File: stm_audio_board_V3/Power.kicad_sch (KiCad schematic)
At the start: 100 parts, among them J5 Barrel_Jack_MountingPin, U1 IS42S16100H-7TL, U2 OP275, U3 7909, U4 OP275, U5 MIC2920A-3.3WS-TR, U6 7809, U9 MIC2920A-3.3WS-TR

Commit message: minor commit
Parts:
- removed C2: 47uf, Capacitor_THT:CP_Radial_D6.3mm_P2.50mm, symbol Device:C_Polarized_Small_US
- removed U5: MIC2920A-3.3WS-TR, Package_TO_SOT_SMD:SOT-223-3_TabPin2, symbol Regulator_Linear:LF33_TO252
- removed U9: MIC2920A-3.3WS-TR, Package_TO_SOT_SMD:SOT-89-3, symbol Regulator_Linear:LF33_TO252
- added C30 (x12): 10uF, Capacitor_SMD:C_1206_3216Metric, symbol Device:C_Small
- added C30: 100n, Capacitor_SMD:C_0603_1608Metric, symbol Device:C_Small
- added U20, U5: AP1117-33, Package_TO_SOT_SMD:SOT-223-3_TabPin2, symbol Regulator_Linear:AP1117-33
- C29: value 100uF -> 100uf
- C29: value 47uF -> 100uf
- U3: JLCPCB (none) -> C8623
- U6: JLCPCB (none) -> C5451665
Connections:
- net +3.3V: now also C29.1, C30.1, C30.1, C30.1, U20.2 (VO)
- net +3.3VA: now also C30.1, C30.1, U5.2 (VO)
- net 5V: now also C30.1, C30.1, C30.1, C30.1, C30.1, U20.3 (VI); no longer C29.1
- net GND: now also C30.2, C30.2, C30.2, C30.2, C30.2, C30.2, C30.2, C30.2, C30.2, C30.2, C30.2, C30.2, C30.2, U20.1 (GND), U5.1 (GND)
- net at C29.1, L5.2: now also C30.1, C30.1, C30.1, U5.3 (VI)
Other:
- note removed: "C157412"
- note removed: "L78M09ABDT-TR"
- note removed: "https://jlcpcb.com/partdetail/Stmicroelectronics-L78M09ABDTTR/C157412"
- moved on the sheet: C29, C3, C30, C4, L5, TP6

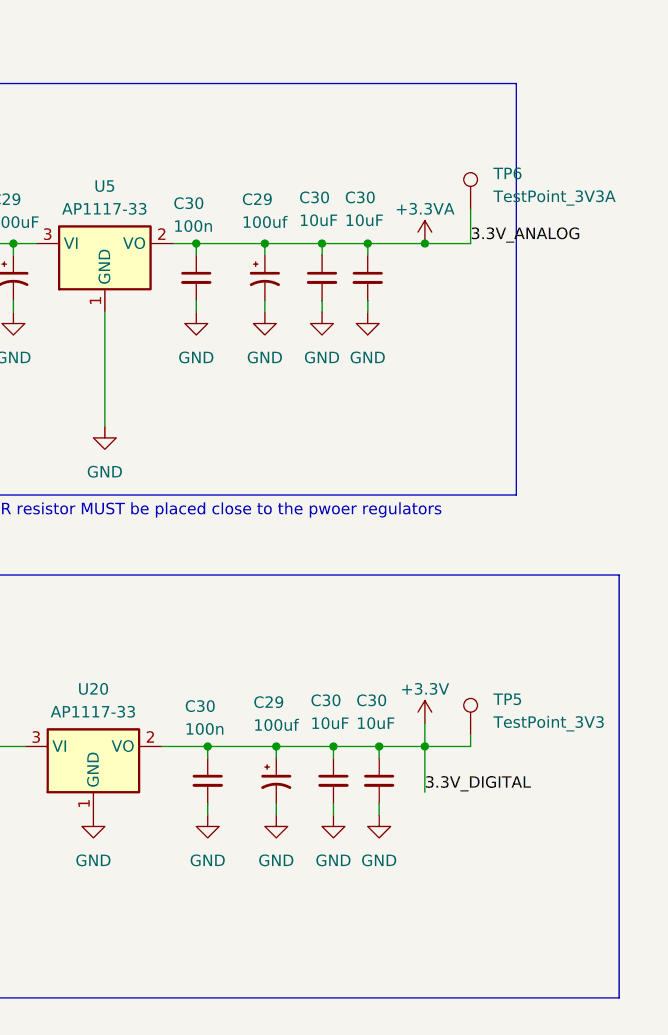
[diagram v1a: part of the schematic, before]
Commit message: gnd vias added, footswitch mux connected
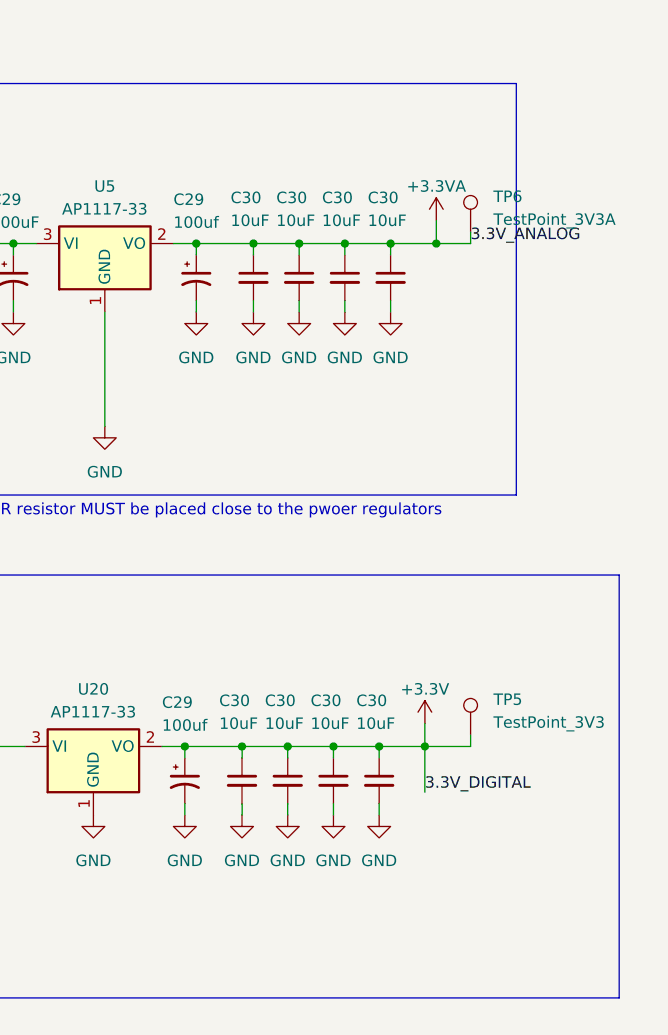
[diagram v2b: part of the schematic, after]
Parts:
- removed C30 (x2): 100n, Capacitor_SMD:C_0603_1608Metric, symbol Device:C_Small
- added C30 (x4): 10uF, Capacitor_SMD:C_1206_3216Metric, symbol Device:C_Small
- U20, U5: footprint Package_TO_SOT_SMD:SOT-223-3_TabPin2 -> Package_TO_SOT_SMD:SOT-223
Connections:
- net +3.3V: now also C30.1, C30.1
- net +3.3VA: now also C30.1, C30.1
- net GND: now also C30.2, C30.2, C30.2, C30.2
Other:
- moved on the sheet: C29, C30, TP6

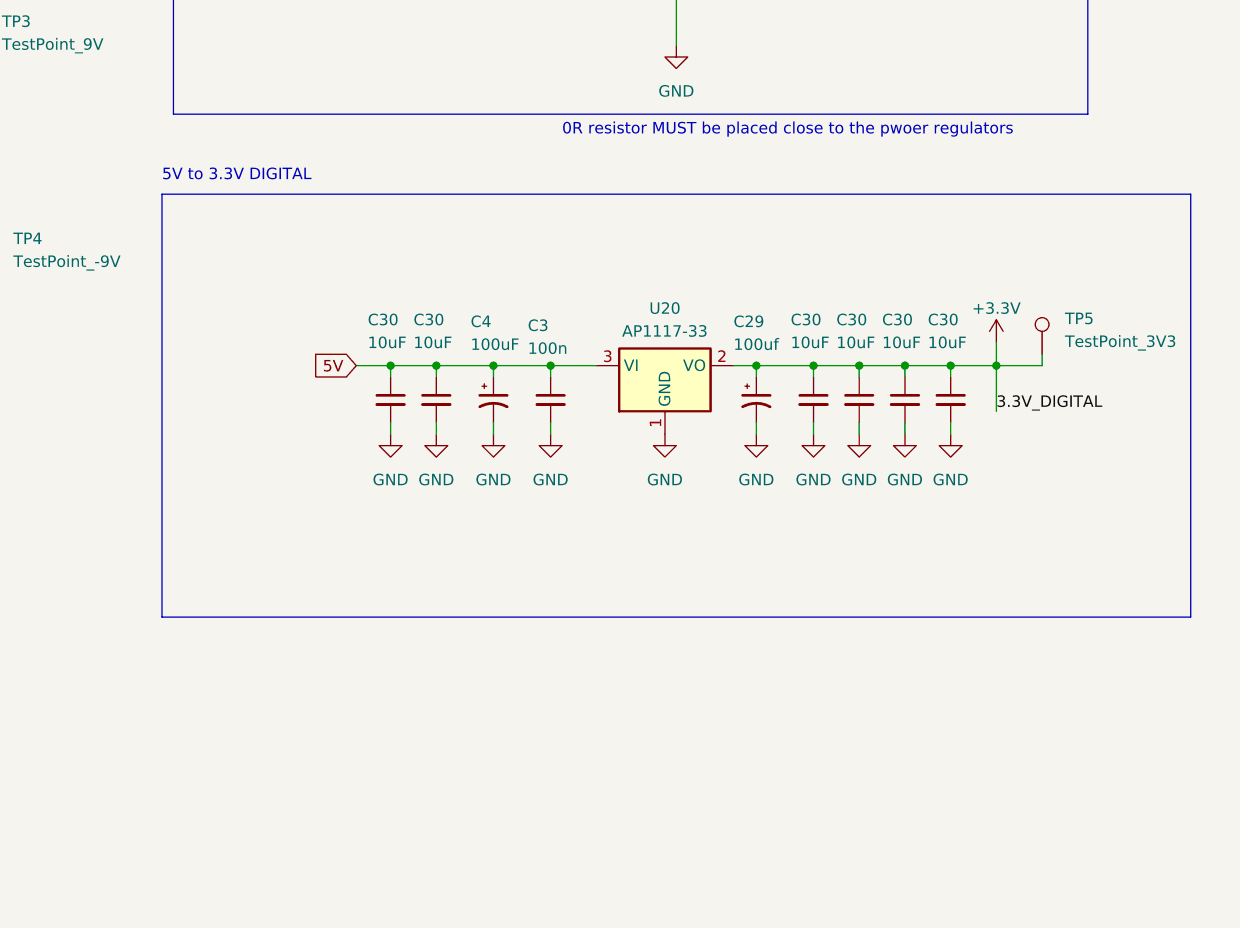
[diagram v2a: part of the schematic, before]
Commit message: added external pot, added feedback leds, added I2C between MCUs
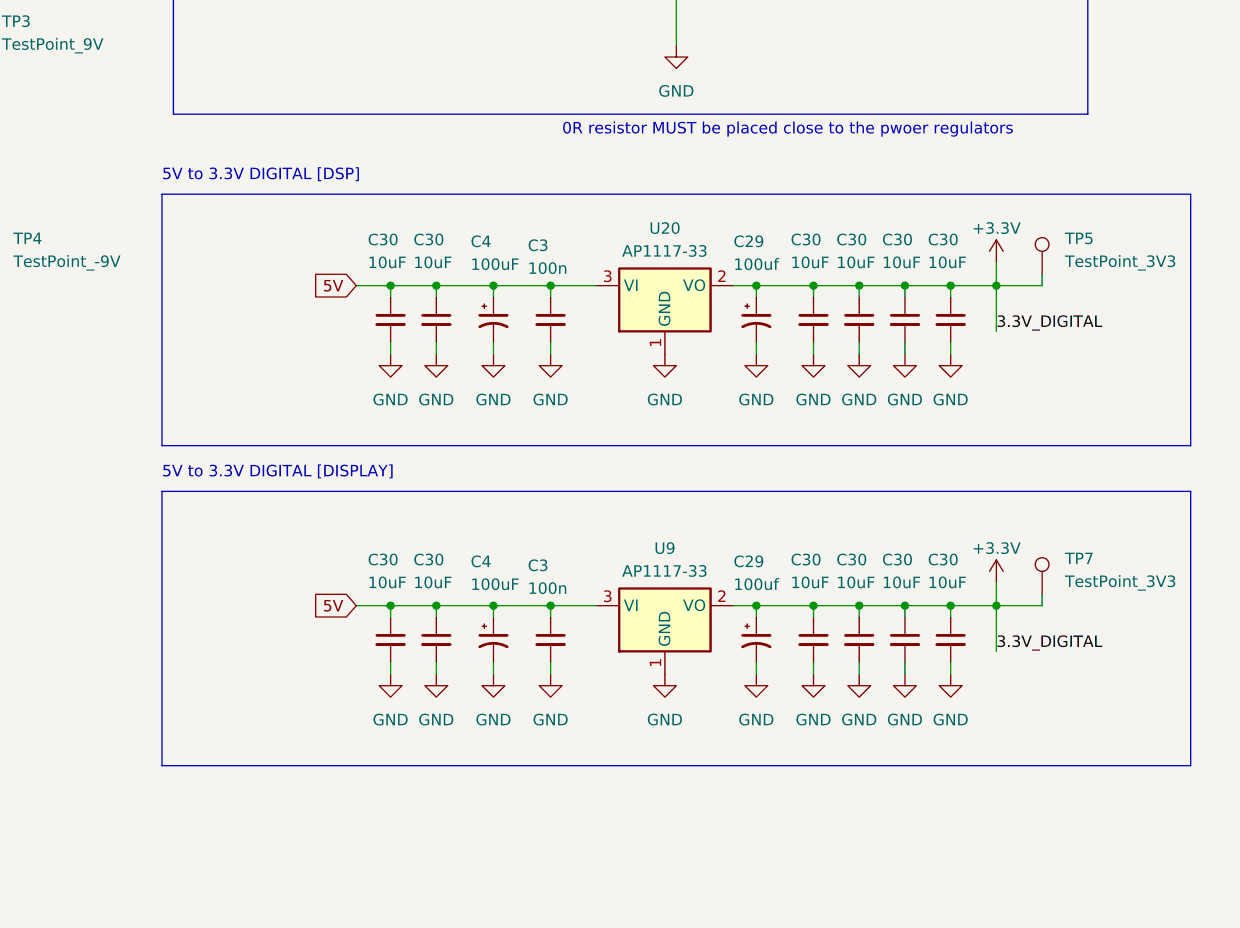
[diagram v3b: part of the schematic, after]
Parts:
- added C29: 100uf, Capacitor_THT:CP_Radial_D6.3mm_P2.50mm, symbol Device:C_Polarized_Small_US
- added C3: 100n, Capacitor_SMD:C_0603_1608Metric, symbol Device:C_Small
- added C30 (x6): 10uF, Capacitor_SMD:C_1206_3216Metric, symbol Device:C_Small
- added C4: 100uF, Capacitor_THT:CP_Radial_D6.3mm_P2.50mm, symbol Device:C_Polarized_Small_US
- added TP7: TestPoint_3V3, TestPoint:TestPoint_Pad_D1.5mm, symbol Connector:TestPoint
- added U9: AP1117-33, Package_TO_SOT_SMD:SOT-223, symbol Regulator_Linear:AP1117-33
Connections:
- net +3.3V: now also C29.1, C30.1, C30.1, C30.1, C30.1, TP7.1, U9.2 (VO)
- net 5V: now also C3.1, C30.1, C30.1, C4.1, U9.3 (VI)
- net GND: now also C29.2, C3.2, C30.2, C30.2, C30.2, C30.2, C30.2, C30.2, C4.2, U9.1 (GND)
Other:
- note added: "5V to 3.3V DIGITAL [DISPLAY]"
- note added: "5V to 3.3V DIGITAL [DSP]"
- note removed: "5V to 3.3V DIGITAL"
- moved on the sheet: C29, C3, C30, C4, TP5, U20

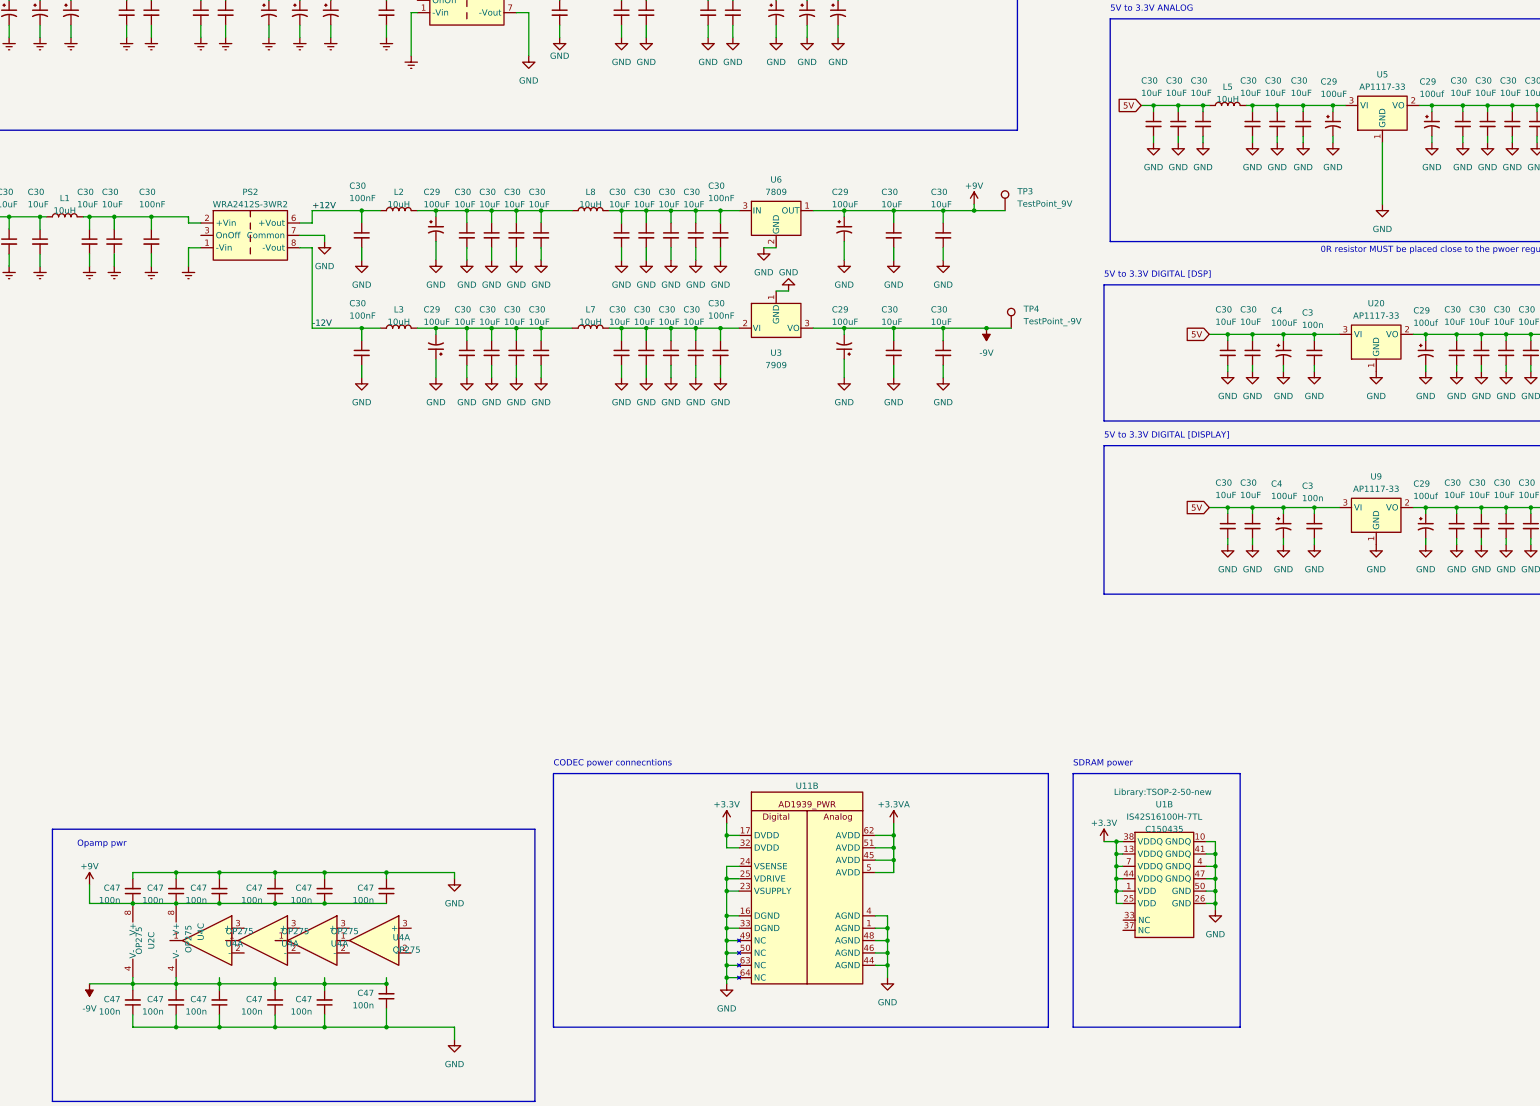
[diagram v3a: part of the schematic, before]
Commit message: minor changes to components
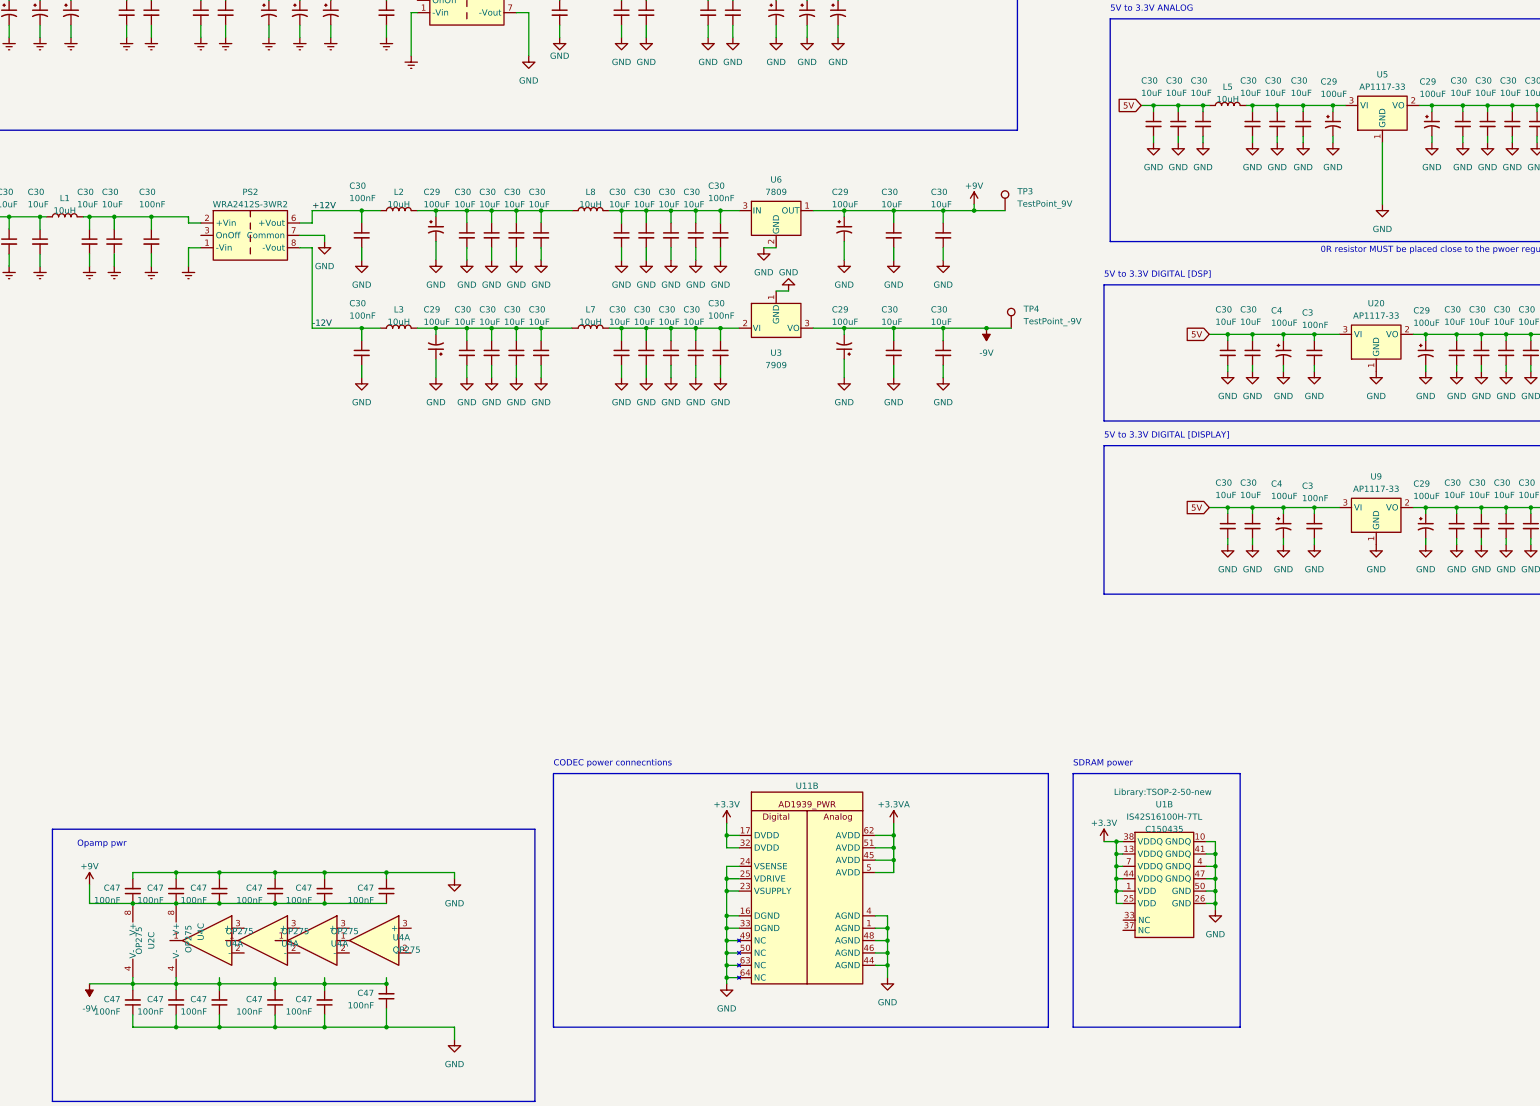
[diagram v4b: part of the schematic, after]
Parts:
- C29, C4: JLCPCB (none) -> C2831718; LCSC Part (none) -> C2831718
- C29: value 100uf -> 100uF; JLCPCB (none) -> C2831718; LCSC Part (none) -> C2831718
- C3, C47: value 100n -> 100nF; JLCPCB (none) -> C14663; LCSC Part (none) -> C14663
- C30: JLCPCB (none) -> C13585; LCSC Part (none) -> C13585
- C30: JLCPCB (none) -> C14663; LCSC Part (none) -> C14663
- J5: LCSC Part (none) -> C3010533
- L1, L2, L3, L4, L5, L6, L7, L8: LCSC Part (none) -> C242335
- PS1: JLCPCB C969036 -> C969046; LCSC Part (none) -> C969046
- PS2: LCSC Part (none) -> C5369662
- U1: LCSC Part (none) -> C150435
- U11: LCSC Part (none) -> C2913556
- U2, U4: LCSC Part (none) -> C161797
- U20, U5, U9: LCSC Part (none) -> C6186
- U3: LCSC Part (none) -> C8623
- U6: LCSC Part (none) -> C5451665
